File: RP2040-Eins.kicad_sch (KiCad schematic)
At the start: 44 parts, among them J1 Barrel_Jack_Switch, J5 CONN_R3, J6 USB_B_Micro, J7 CONN_JTAG, Q1 AO3401A, SW1 BOOTSEL, SW2 RESET, U1 W25Q128JVS, U2 RP2040, U3 AMS1117-5.0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

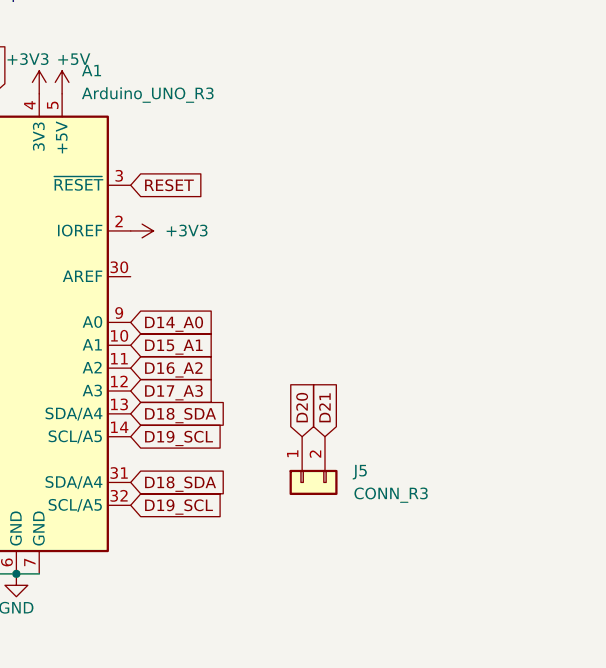
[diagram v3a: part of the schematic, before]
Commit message: Added ICSP connector. Changed JTAG connector footprint.
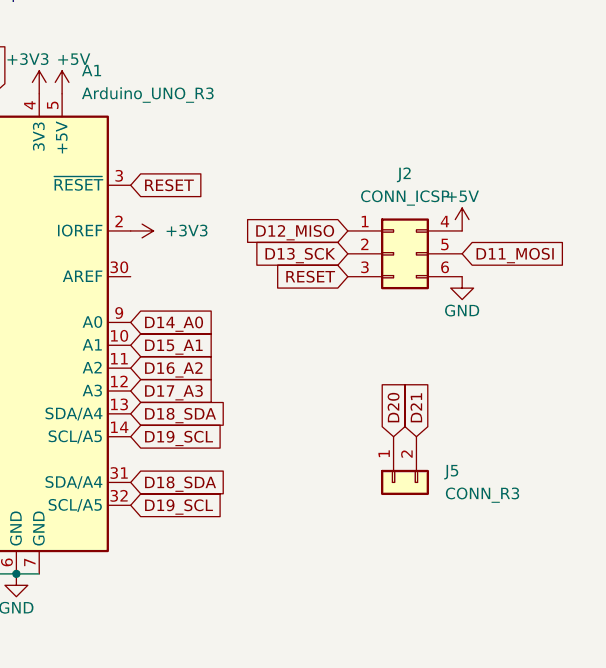
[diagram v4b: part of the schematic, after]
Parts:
- added J2: CONN_ICSP, Connector_PinSocket_2.54mm:PinSocket_2x03_P2.54mm_Vertical, symbol Connector_Generic:Conn_02x03_Top_Bottom
- J5: footprint Connector_PinHeader_2.54mm:PinHeader_1x02_P2.54mm_Vertical -> Connector_PinSocket_2.54mm:PinSocket_1x02_P2.54mm_Vertical
- J7: footprint Connector_PinHeader_1.27mm:PinHeader_2x05_P1.27mm_Vertical_SMD -> Connector_PinHeader_1.27mm:PinHeader_2x05_P1.27mm_Vertical
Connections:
- net +5V: now also J2.4 (Pin_4)
- net D11_MOSI: now also J2.5 (Pin_5)
- net D12_MISO: now also J2.1 (Pin_1)
- net D13_SCK: now also J2.2 (Pin_2)
- net GND: now also J2.6 (Pin_6)
- net RESET: now also J2.3 (Pin_3)
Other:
- moved on the sheet: J5
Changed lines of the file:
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@@
   (title_block
     (title "RP2040-Eins-0010")
-    (date "2023-09-20")
+    (date "2023-09-22")
     (rev "1.0")
     (company "(c) 2023 Andriy Golovnya")
@@
     )
   )
-  (global_label "D20" (shape input) (at 254 71.12 90) (fields_autoplaced)
-    (effects (font (size 1.27 1.27)) (justify left))
-    (property "Intersheetrefs" "${INTERSHEET_REFS}" (at 254 64.5252 90)
+  (global_label "D12_MISO" (shape input) (at 259.08 48.26 180) (fields_autoplaced)
+    (effects (font (size 1.27 1.27)) (justify right))
+    (property "Intersheetrefs" "${INTERSHEET_REFS}" (at 246.842 48.26 0)
+      (effects (font (size 1.27 1.27)) (justify right) hide)
+    )
+  )
+  (global_label "D20" (shape input) (at 264.16 71.12 90) (fields_autoplaced)
+    (effects (font (size 1.27 1.27)) (justify left))
+    (property "Intersheetrefs" "${INTERSHEET_REFS}" (at 264.16 64.5252 90)
       (effects (font (size 1.27 1.27)) (justify left) hide)
     )
@@
     )
   )
+  (global_label "D11_MOSI" (shape input) (at 271.78 50.8 0) (fields_autoplaced)
+    (effects (font (size 1.27 1.27)) (justify left))
+    (property "Intersheetrefs" "${INTERSHEET_REFS}" (at 284.018 50.8 0)
+      (effects (font (size 1.27 1.27)) (justify left) hide)
+    )
+  )
   (global_label "D7" (shape input) (at 209.55 60.96 180) (fields_autoplaced)
     (effects (font (size 1.27 1.27)) (justify right))
@@
     )
   )
+  (global_label "D13_SCK" (shape input) (at 259.08 50.8 180) (fields_autoplaced)
+    (effects (font (size 1.27 1.27)) (justify right))
+    (property "Intersheetrefs" "${INTERSHEET_REFS}" (at 247.6887 50.8 0)
+      (effects (font (size 1.27 1.27)) (justify right) hide)
+    )
+  )
   (global_label "D19_SCL" (shape input) (at 234.95 71.12 0) (fields_autoplaced)
     (effects (font (size 1.27 1.27)) (justify left))
@@
     )
   )
+  (global_label "RESET" (shape input) (at 259.08 53.34 180) (fields_autoplaced)
+    (effects (font (size 1.27 1.27)) (justify right))
+    (property "Intersheetrefs" "${INTERSHEET_REFS}" (at 250.3497 53.34 0)
+      (effects (font (size 1.27 1.27)) (justify right) hide)
+    )
+  )
   (global_label "D8" (shape input) (at 166.37 88.9 0) (fields_autoplaced)
     (effects (font (size 1.27 1.27)) (justify left))
@@
     )
   )
-  (global_label "D21" (shape input) (at 256.54 71.12 90) (fields_autoplaced)
-    (effects (font (size 1.27 1.27)) (justify left))
-    (property "Intersheetrefs" "${INTERSHEET_REFS}" (at 256.54 64.5252 90)
+  (global_label "D21" (shape input) (at 266.7 71.12 90) (fields_autoplaced)
+    (effects (font (size 1.27 1.27)) (justify left))
+    (property "Intersheetrefs" "${INTERSHEET_REFS}" (at 266.7 64.5252 90)
       (effects (font (size 1.27 1.27)) (justify left) hide)
     )
@@
     )
   )
-  (symbol (lib_id "Connector_Generic:Conn_01x02") (at 254 76.2 90) (mirror x) (unit 1)
-    (in_bom yes) (on_board yes) (dnp no)
-    (property "Reference" "J5" (at 259.715 74.93 90)
+  (symbol (lib_id "Connector_Generic:Conn_01x02") (at 264.16 76.2 90) (mirror x) (unit 1)
+    (in_bom yes) (on_board yes) (dnp no)
+    (property "Reference" "J5" (at 269.875 74.93 90)
       (effects (font (size 1.27 1.27)) (justify right))
     )
-    (property "Value" "CONN_R3" (at 259.715 77.47 90)
+    (property "Value" "CONN_R3" (at 269.875 77.47 90)
       (effects (font (size 1.27 1.27)) (justify right))
     )
-    (property "Footprint" "Connector_PinHeader_2.54mm:PinHeader_1x02_P2.54mm_Vertical" (at 254 76.2 0)
-      (effects (font (size 1.27 1.27)) hide)
-    )
-    (property "Datasheet" "~" (at 254 76.2 0)
+    (property "Footprint" "Connector_PinSocket_2.54mm:PinSocket_1x02_P2.54mm_Vertical" (at 264.16 76.2 0)
+      (effects (font (size 1.27 1.27)) hide)
+    )
+    (property "Datasheet" "~" (at 264.16 76.2 0)
       (effects (font (size 1.27 1.27)) hide)
     )
@@
         (path "/9a38a81c-7302-494f-9784-2ab4342a0a1d"
           (reference "#PWR025") (unit 1)
+        )
+      )
+    )
+  )
+  (symbol (lib_id "power:GND") (at 271.78 53.34 0) (unit 1)
+    (in_bom yes) (on_board yes) (dnp no)
+    (property "Reference" "#PWR068" (at 271.78 59.69 0)
+      (effects (font (size 1.27 1.27)) hide)
+    )
+    (property "Value" "GND" (at 271.78 57.15 0)
+      (effects (font (size 1.27 1.27)))
+    )
+    (property "Footprint" "" (at 271.78 53.34 0)
+      (effects (font (size 1.27 1.27)) hide)
+    )
+    (property "Datasheet" "" (at 271.78 53.34 0)
+      (effects (font (size 1.27 1.27)) hide)
+    )
+    (pin "1")
+    (instances
+      (project "RP2040-Eins"
+        (path "/9a38a81c-7302-494f-9784-2ab4342a0a1d"
+          (reference "#PWR068") (unit 1)
         )
       )
@@
       (effects (font (size 1.27 1.27)) (justify right))
     )
-    (property "Footprint" "Connector_PinHeader_1.27mm:PinHeader_2x05_P1.27mm_Vertical_SMD" (at 40.64 172.72 0)
+    (property "Footprint" "Connector_PinHeader_1.27mm:PinHeader_2x05_P1.27mm_Vertical" (at 40.64 172.72 0)
       (effects (font (size 1.27 1.27)) hide)
     )
@@
     )
   )
+  (symbol (lib_id "power:+5V") (at 271.78 48.26 0) (unit 1)
+    (in_bom yes) (on_board yes) (dnp no)
+    (property "Reference" "#PWR069" (at 271.78 52.07 0)
+      (effects (font (size 1.27 1.27)) hide)
+    )
+    (property "Value" "+5V" (at 271.78 44.45 0)
+      (effects (font (size 1.27 1.27)))
+    )
+    (property "Footprint" "" (at 271.78 48.26 0)
+      (effects (font (size 1.27 1.27)) hide)
+    )
+    (property "Datasheet" "" (at 271.78 48.26 0)
+      (effects (font (size 1.27 1.27)) hide)
+    )
+    (pin "1")
+    (instances
+      (project "RP2040-Eins"
+        (path "/9a38a81c-7302-494f-9784-2ab4342a0a1d"
+          (reference "#PWR069") (unit 1)
+        )
+      )
+    )
+  )
   (symbol (lib_id "Regulator_Linear:AMS1117-5.0") (at 215.9 139.7 0) (unit 1)
     (in_bom yes) (on_board yes) (dnp no) (fields_autoplaced)
@@
         )
       )
+    )
+  )
+  (symbol (lib_id "Connector_Generic:Conn_02x03_Top_Bottom") (at 264.16 50.8 0) (unit 1)
+    (in_bom yes) (on_board yes) (dnp no) (fields_autoplaced)
+    (property "Reference" "J2" (at 265.43 41.91 0)
+      (effects (font (size 1.27 1.27)))
+    )
+    (property "Value" "CONN_ICSP" (at 265.43 44.45 0)
+      (effects (font (size 1.27 1.27)))
+    )
+    (property "Footprint" "Connector_PinSocket_2.54mm:PinSocket_2x03_P2.54mm_Vertical" (at 264.16 50.8 0)
+      (effects (font (size 1.27 1.27)) hide)
+    )
+    (property "Datasheet" "~" (at 264.16 50.8 0)
+      (effects (font (size 1.27 1.27)) hide)
+    )
+    (pin "1")
+    (pin "2")
+    (pin "3")
+    (pin "4")
+    (pin "5")
+    (pin "6")
+    (instances
+      (project "RP2040-Eins"
+        (path "/9a38a81c-7302-494f-9784-2ab4342a0a1d"
+          (reference "J2") (unit 1)
+        )
+      )

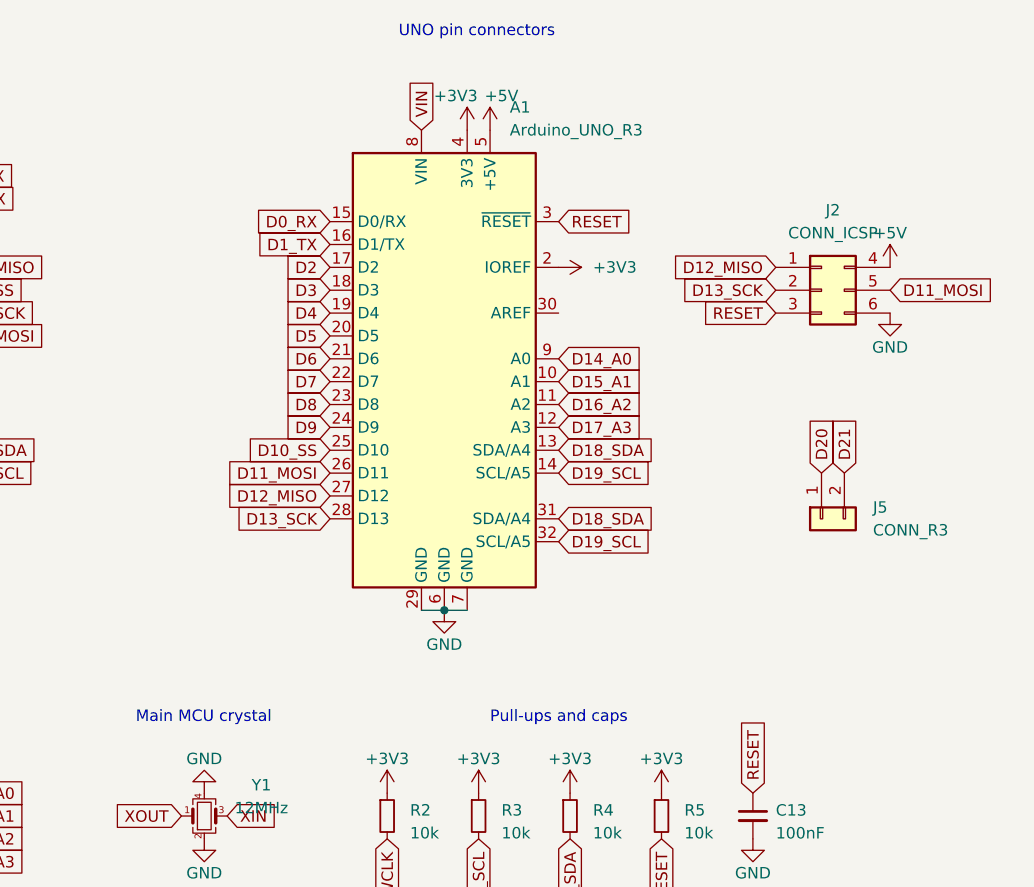
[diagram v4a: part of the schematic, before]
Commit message: Exchanged Arduino board shape with separate connectors
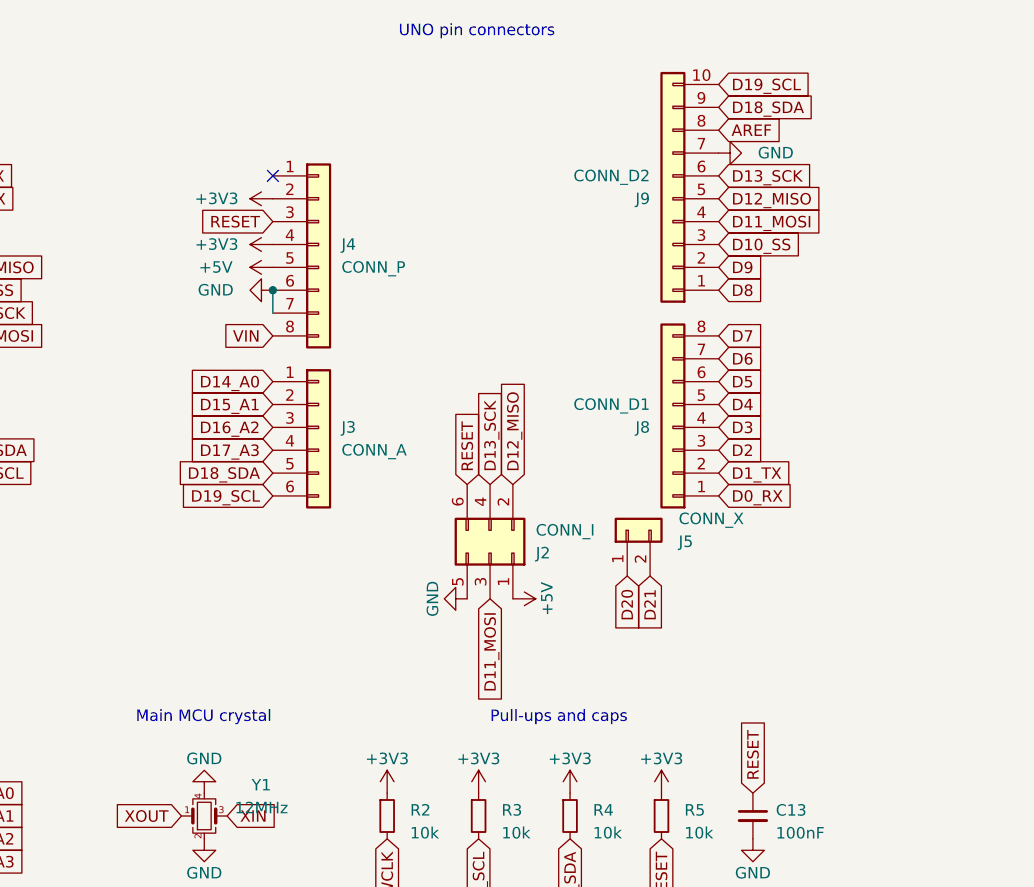
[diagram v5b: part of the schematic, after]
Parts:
- removed A1: Arduino_UNO_R3, Module:Arduino_UNO_R3_WithMountingHoles, symbol MCU_Module:Arduino_UNO_R3
- removed J2: CONN_ICSP, Connector_PinSocket_2.54mm:PinSocket_2x03_P2.54mm_Vertical, symbol Connector_Generic:Conn_02x03_Top_Bottom
- added J2: CONN_I, Connector_PinSocket_2.54mm:PinSocket_2x03_P2.54mm_Vertical, symbol Connector_Generic:Conn_02x03_Odd_Even
- added J3: CONN_A, Connector_PinSocket_2.54mm:PinSocket_1x06_P2.54mm_Vertical, symbol Connector_Generic:Conn_01x06
- added J4: CONN_P, Connector_PinSocket_2.54mm:PinSocket_1x08_P2.54mm_Vertical, symbol Connector_Generic:Conn_01x08
- added J8: CONN_D1, Connector_PinSocket_2.54mm:PinSocket_1x08_P2.54mm_Vertical, symbol Connector_Generic:Conn_01x08
- added J9: CONN_D2, Connector_PinSocket_2.54mm:PinSocket_1x10_P2.54mm_Vertical, symbol Connector_Generic:Conn_01x10
- J5: value CONN_R3 -> CONN_X
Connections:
- net +3V3: now also J4.2 (Pin_2), J4.4 (Pin_4)
- net +5V: now also J2.1 (Pin_1), J4.5 (Pin_5)
- net D0_RX: now also J8.1 (Pin_1)
- net D10_SS: now also J9.3 (Pin_3)
- net D11_MOSI: now also J2.3 (Pin_3), J9.4 (Pin_4)
- net D12_MISO: now also J2.2 (Pin_2), J9.5 (Pin_5)
- net D13_SCK: now also J2.4 (Pin_4), J9.6 (Pin_6)
- net D14_A0: now also J3.1 (Pin_1)
- net D15_A1: now also J3.2 (Pin_2)
- net D16_A2: now also J3.3 (Pin_3)
- net D17_A3: now also J3.4 (Pin_4)
- net D18_SDA: now also J3.5 (Pin_5), J9.9 (Pin_9)
- net D19_SCL: now also J3.6 (Pin_6), J9.10 (Pin_10)
- net D1_TX: now also J8.2 (Pin_2)
- net D2: now also J8.3 (Pin_3)
- net D3: now also J8.4 (Pin_4)
- net D4: now also J8.5 (Pin_5)
- net D5: now also J8.6 (Pin_6)
- net D6: now also J8.7 (Pin_7)
- net D7: now also J8.8 (Pin_8)
- net D8: now also J9.1 (Pin_1)
- net D9: now also J9.2 (Pin_2)
- net GND: now also J2.5 (Pin_5), J4.6 (Pin_6), J4.7 (Pin_7), J9.7 (Pin_7)
- net RESET: now also J2.6 (Pin_6), J4.3 (Pin_3)
- net VIN: now also J4.8 (Pin_8)
- new net AREF: J9.8 (Pin_8)
- no-connect marks 12 -> 13
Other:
- moved on the sheet: J5

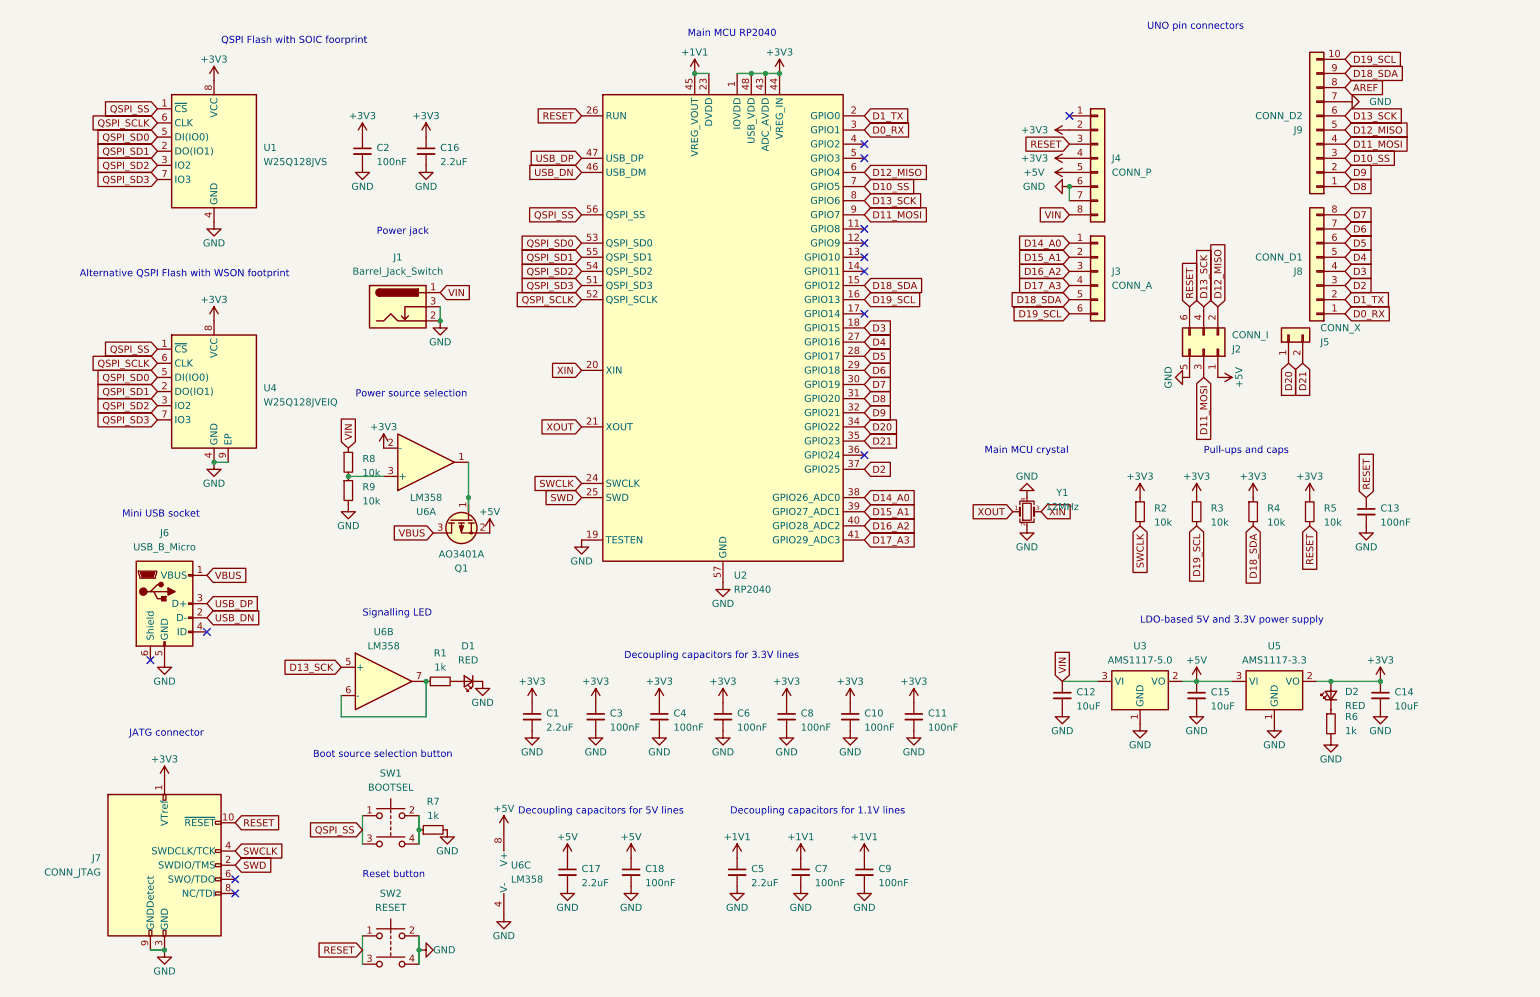
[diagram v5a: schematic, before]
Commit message: Added quartz caps. Moved stuff around.
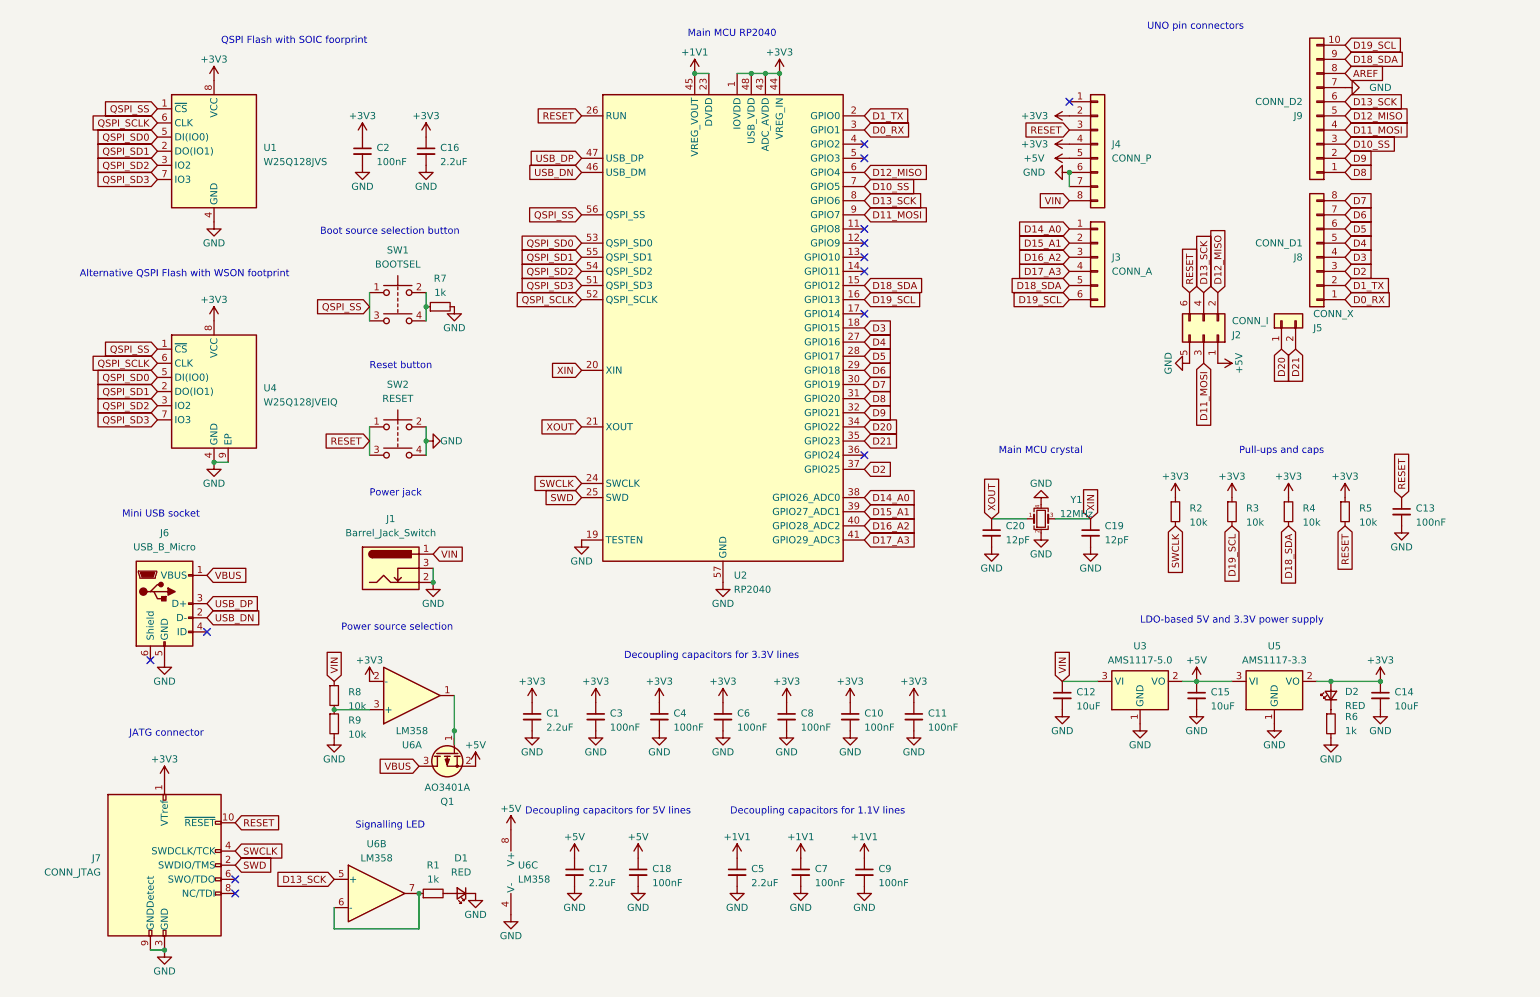
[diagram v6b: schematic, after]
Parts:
- added C19, C20: 12pF, Capacitor_SMD:C_0402_1005Metric, symbol Device:C_Small
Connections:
- net GND: now also C19.2, C20.2
- net XIN: now also C19.1
- net XOUT: now also C20.1
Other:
- moved on the sheet: C13, C17, C18, D1, J1, J2, J3, J4, J5, J8, J9, Q1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
